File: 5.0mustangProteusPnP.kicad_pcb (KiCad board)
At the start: 2 copper layers, 139.7 x 111.1 mm, 6 parts, among them J2 5103308-3, J3 776228-1, J4 5103308-3, J5 776231-2, J6 776231-1, U1 FORD60PIN

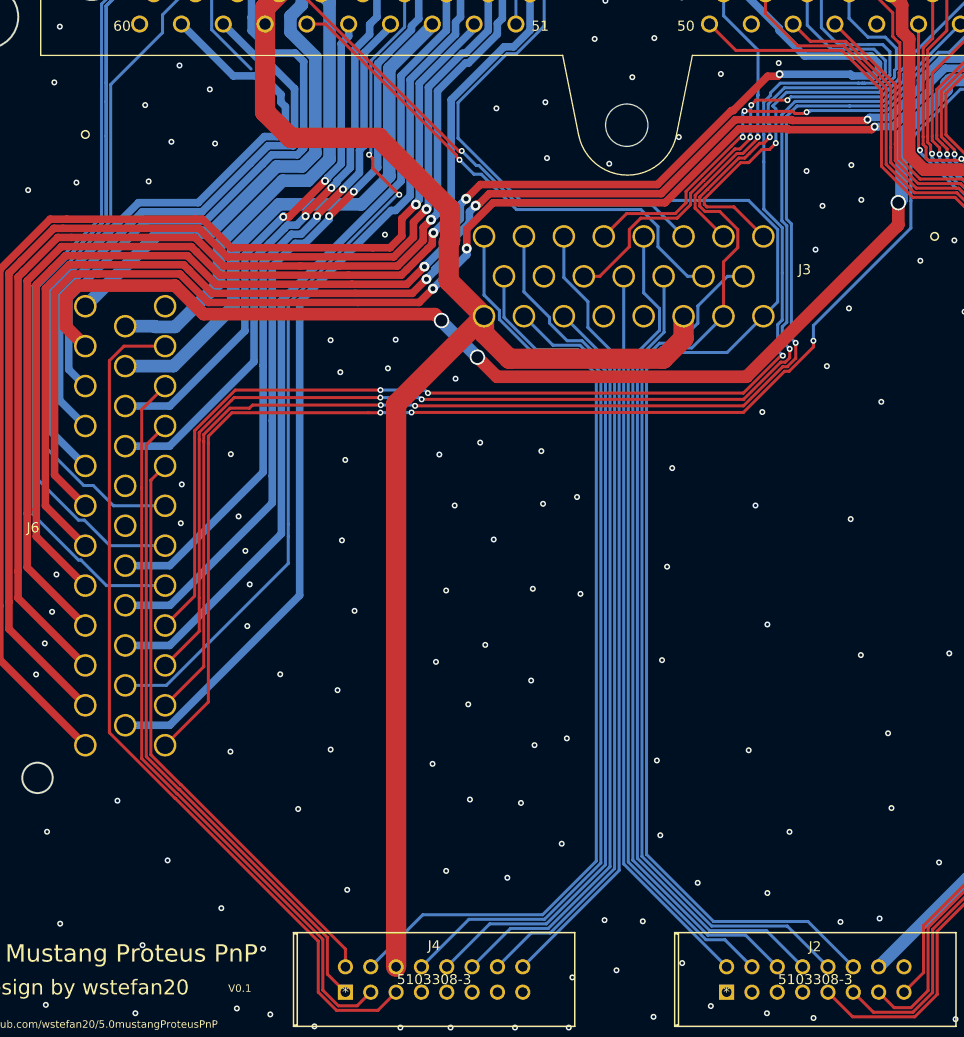
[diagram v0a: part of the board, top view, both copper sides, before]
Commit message: re-routed to optimise
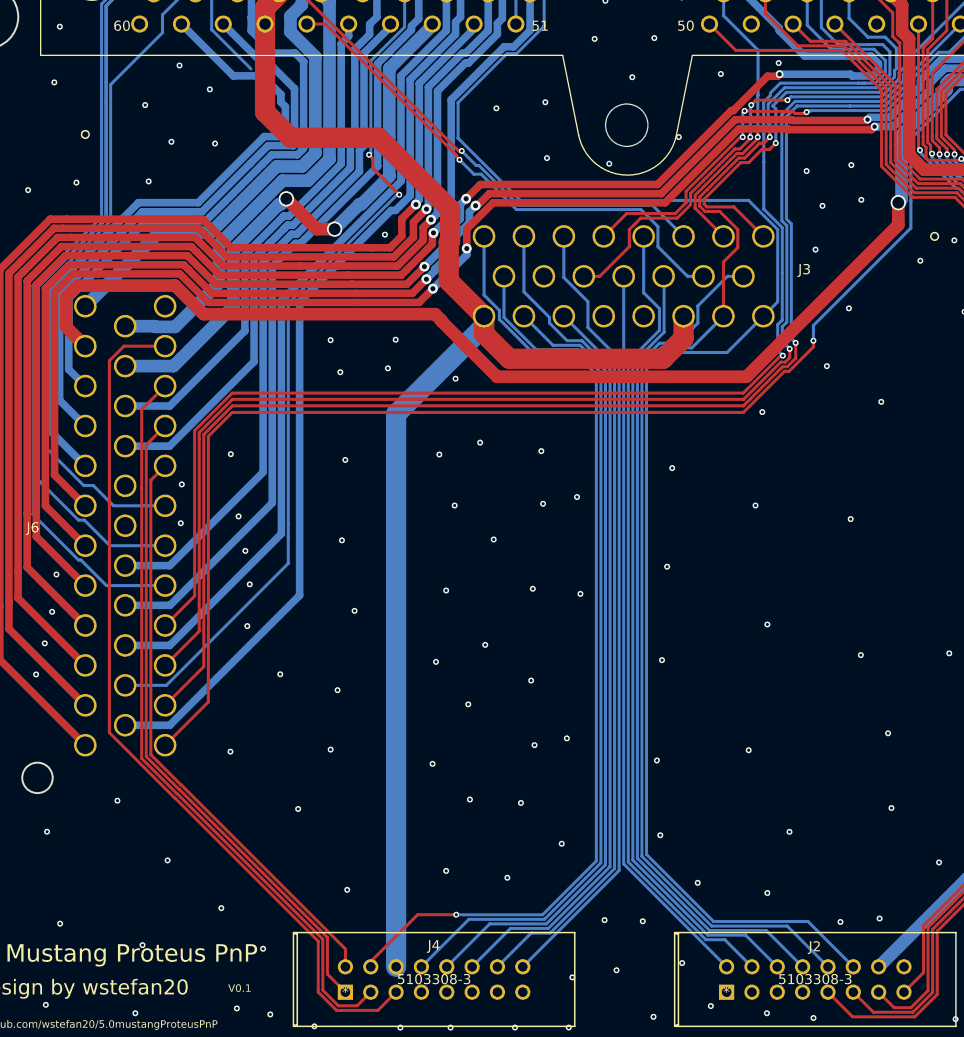
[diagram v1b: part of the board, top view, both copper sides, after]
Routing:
- net /HS4: track 54.7 -> 57.2 mm, vias 0 -> 2
- net /ETB2-: track 96.7 -> 97.0 mm, vias 0 -> 1
- net /LS10: track 79.7 -> 79.4 mm, vias 2 -> 0
- net /LS8: track 68.5 -> 68.2 mm, vias 2 -> 0
- net /IGN5: track 136.9 -> 136.7 mm, vias 3 -> 1
- net /LS4: track 62.0 -> 61.7 mm, vias 2 -> 0
- net /IGN4: track 137.6 -> 137.5 mm, vias 3 -> 1
- net /LS2: track 50.7 -> 50.6 mm, vias 2 -> 0
- net /IGN2: track 137.6 -> 137.5 mm, vias 3 -> 1
- net /IGN1: vias 3 -> 1
- net /HS1: vias 3 -> 1

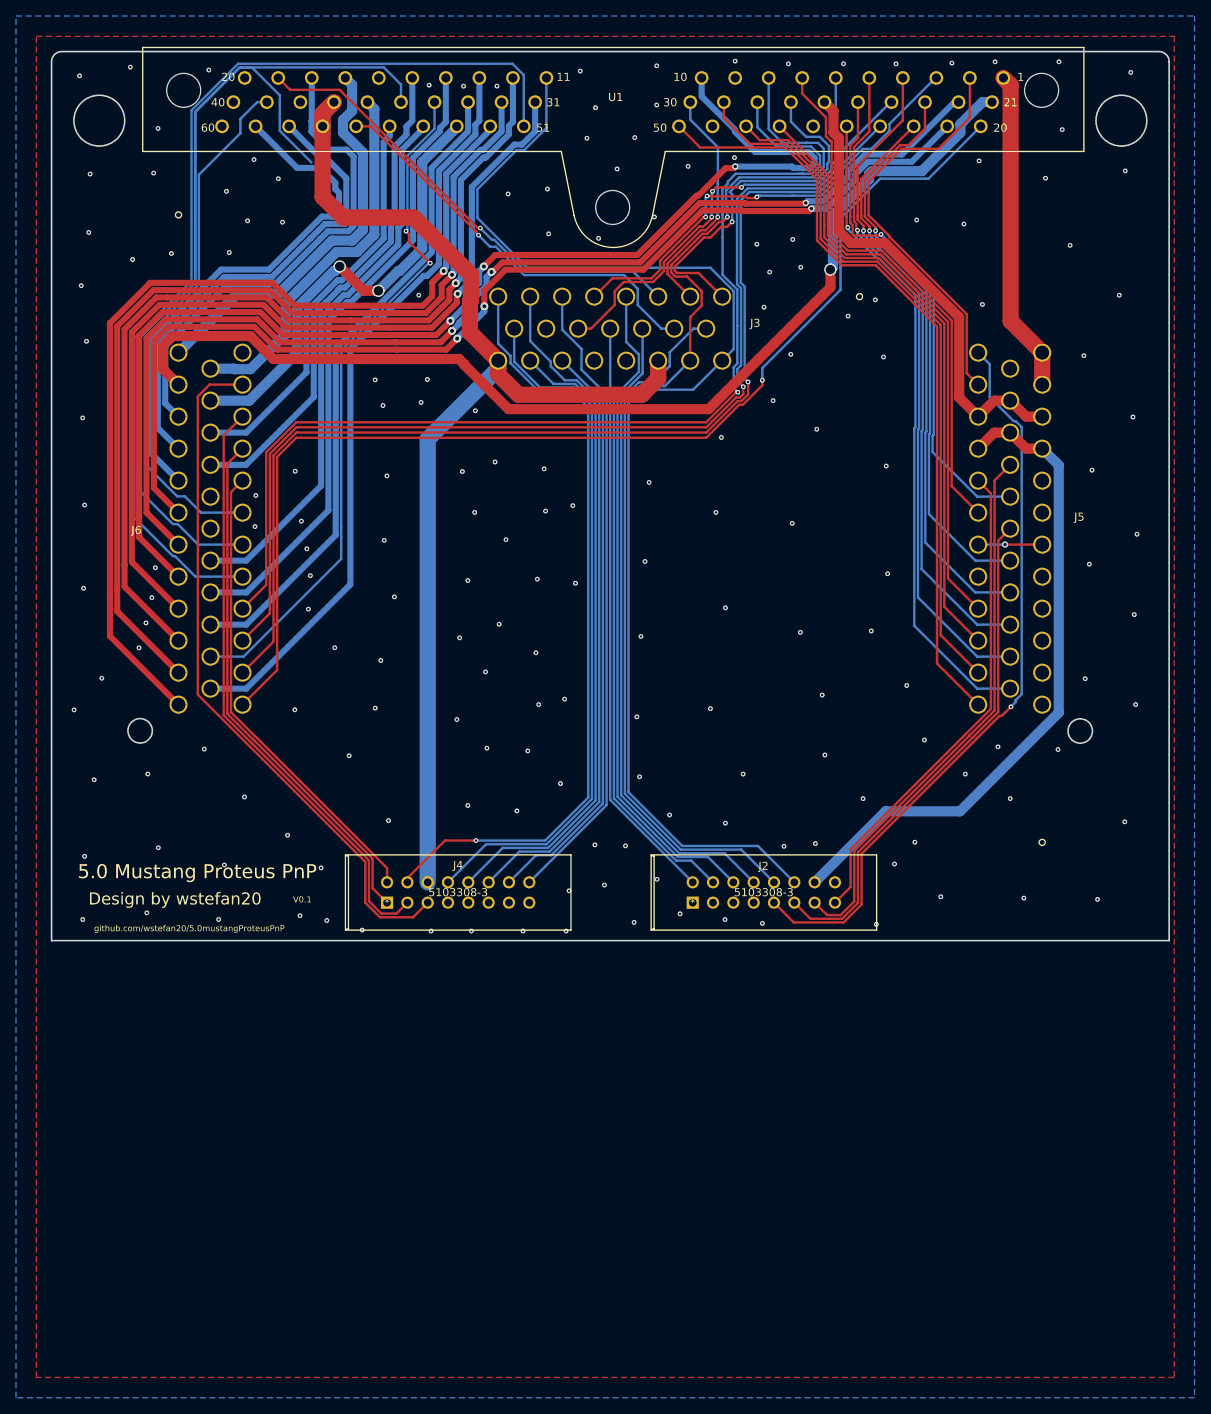
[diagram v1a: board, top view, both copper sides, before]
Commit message: changed 12V
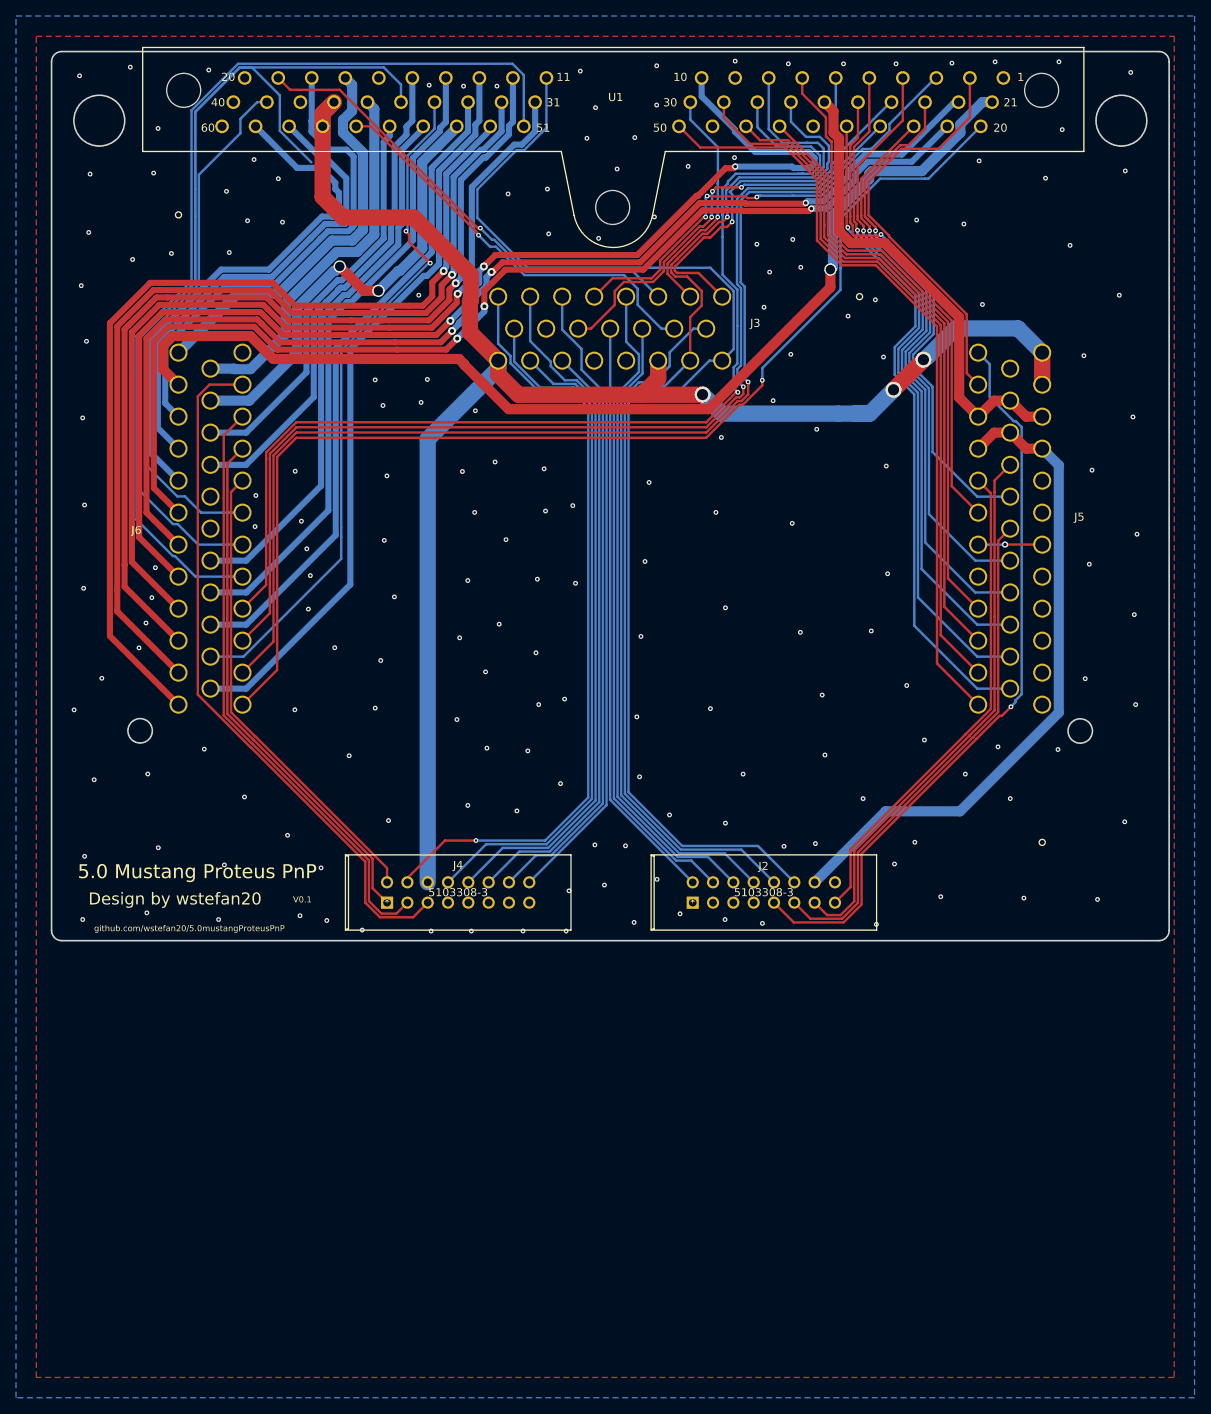
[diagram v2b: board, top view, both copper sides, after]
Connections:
- J5 pad 11: /12V -> /12V_MR
- J5 pad 12: /12V -> /12V_MR
- U1 pad 1: /12V -> (no net)
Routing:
- net /12V_MR: track 142.0 -> 204.0 mm, vias 0 -> 3
- net /12V: track 40.3 -> 0.00 mm
- net /AT1: track 62.7 -> 64.7 mm
- net /AV9: track 71.4 -> 73.4 mm
- net /AV7: track 71.5 -> 73.5 mm
- net /AV5: track 81.3 -> 83.3 mm
- net /AV3: track 83.9 -> 85.9 mm
- net /AV1: track 81.4 -> 83.5 mm
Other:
- outline, holes or cut-outs redrawn

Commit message: fixed 12V and IAC
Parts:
- added J1: 5-146280-3, 5-146280-3:5-146280-3, F.Cu at (222.3, 77.6)
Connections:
- J5 pad 11: /12V_MR -> /MR_INPUT
- J5 pad 12: /12V_MR -> /MR_INPUT
- J6 pad 2: /HS1 -> (no net)
- U1 pad 1: (no net) -> /12V
- U1 pad 21: /HS1 -> /LS14
- U1 pad 32: /LS14 -> (no net)
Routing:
- net /HS1: track 135.6 -> 0.00 mm, vias 1 -> 0
- net /LS14: track 118.6 -> 180.1 mm, vias 1 -> 2
- net /MR_INPUT: track 0.00 -> 27.0 mm
- net /12V: track 0.00 -> 14.5 mm
- net /12V_MR: track 204.0 -> 211.8 mm
- net /LS13: track 117.4 -> 118.0 mm
- net GND: vias 183 -> 204
- net (no net): vias 4 -> 0

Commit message: fixed CEL assign
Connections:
- J2 pad 1: (no net) -> /HS1
- J4 pad 7: (no net) -> /HS2
- J6 pad 2: (no net) -> /HS1
- U1 pad 17: /HS2 -> /LS12
- U1 pad 33: /LS12 -> (no net)
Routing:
- net /HS1: track 0.00 -> 125.7 mm, vias 0 -> 2
- net /HS2: track 50.3 -> 149.3 mm, vias 0 -> 1
- net /IGN7: track 147.9 -> 132.9 mm
- net /LS12: track 81.3 -> 84.1 mm, vias 0 -> 2
- net /HS4: track 57.2 -> 57.8 mm
- net GND: vias 204 -> 205

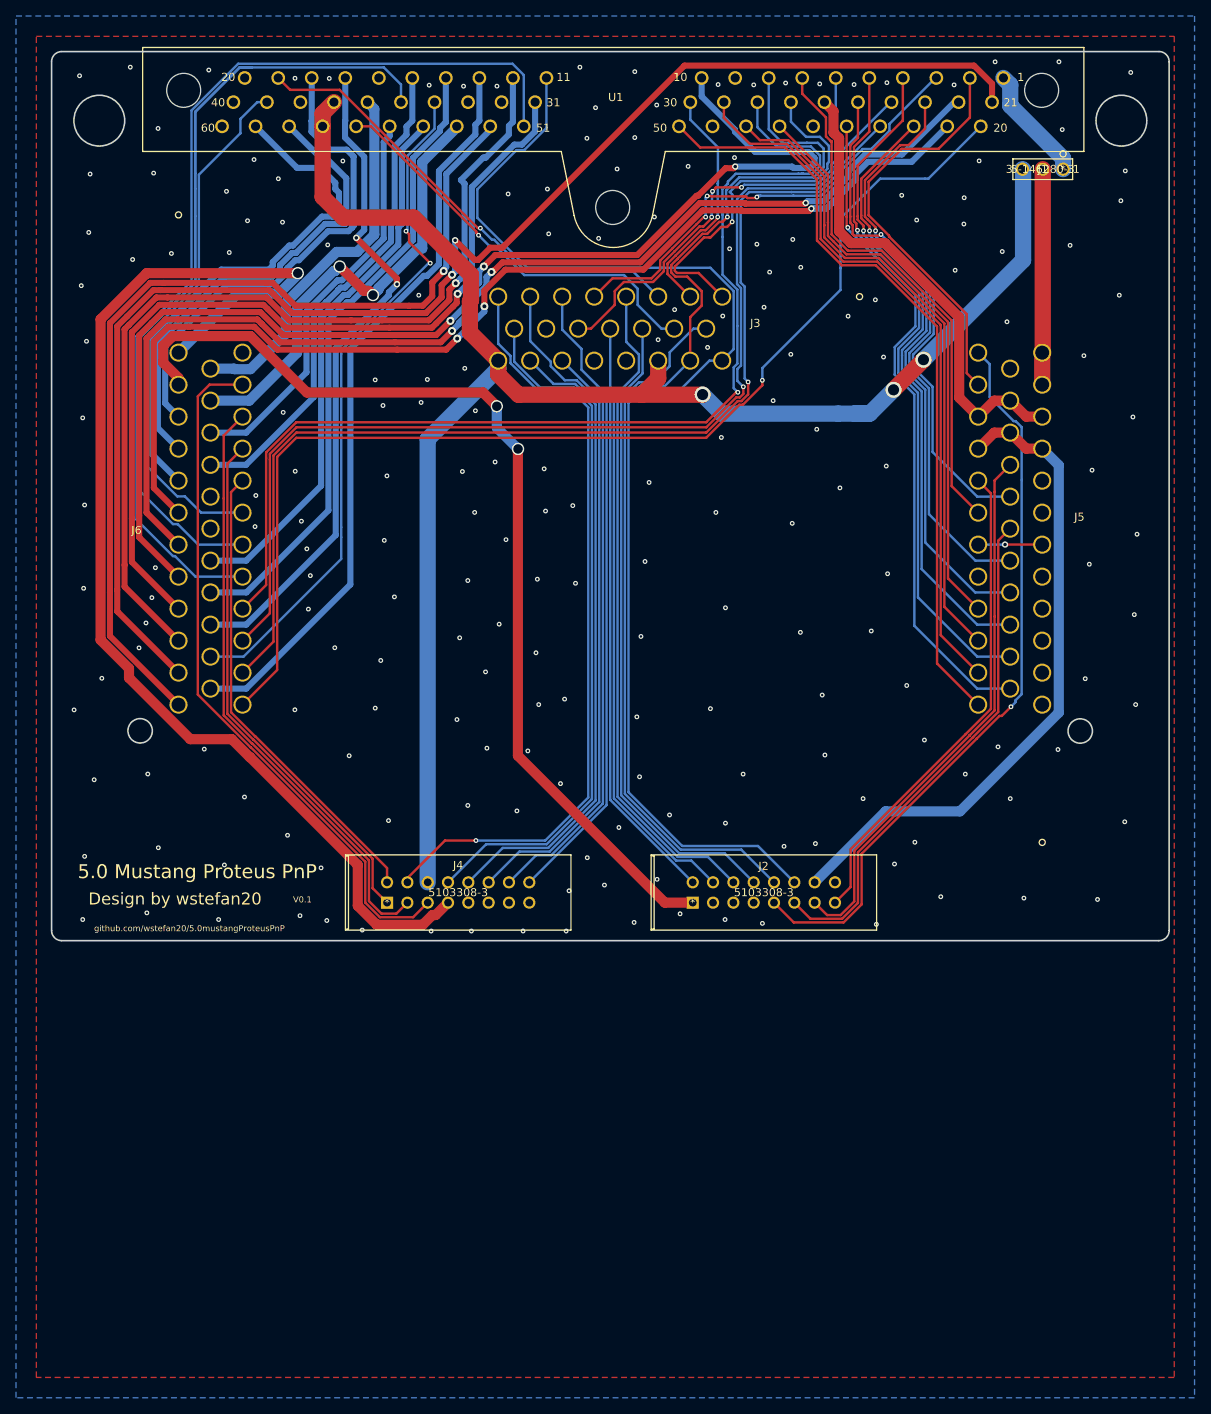
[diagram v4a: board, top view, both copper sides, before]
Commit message: updated board outline/holes
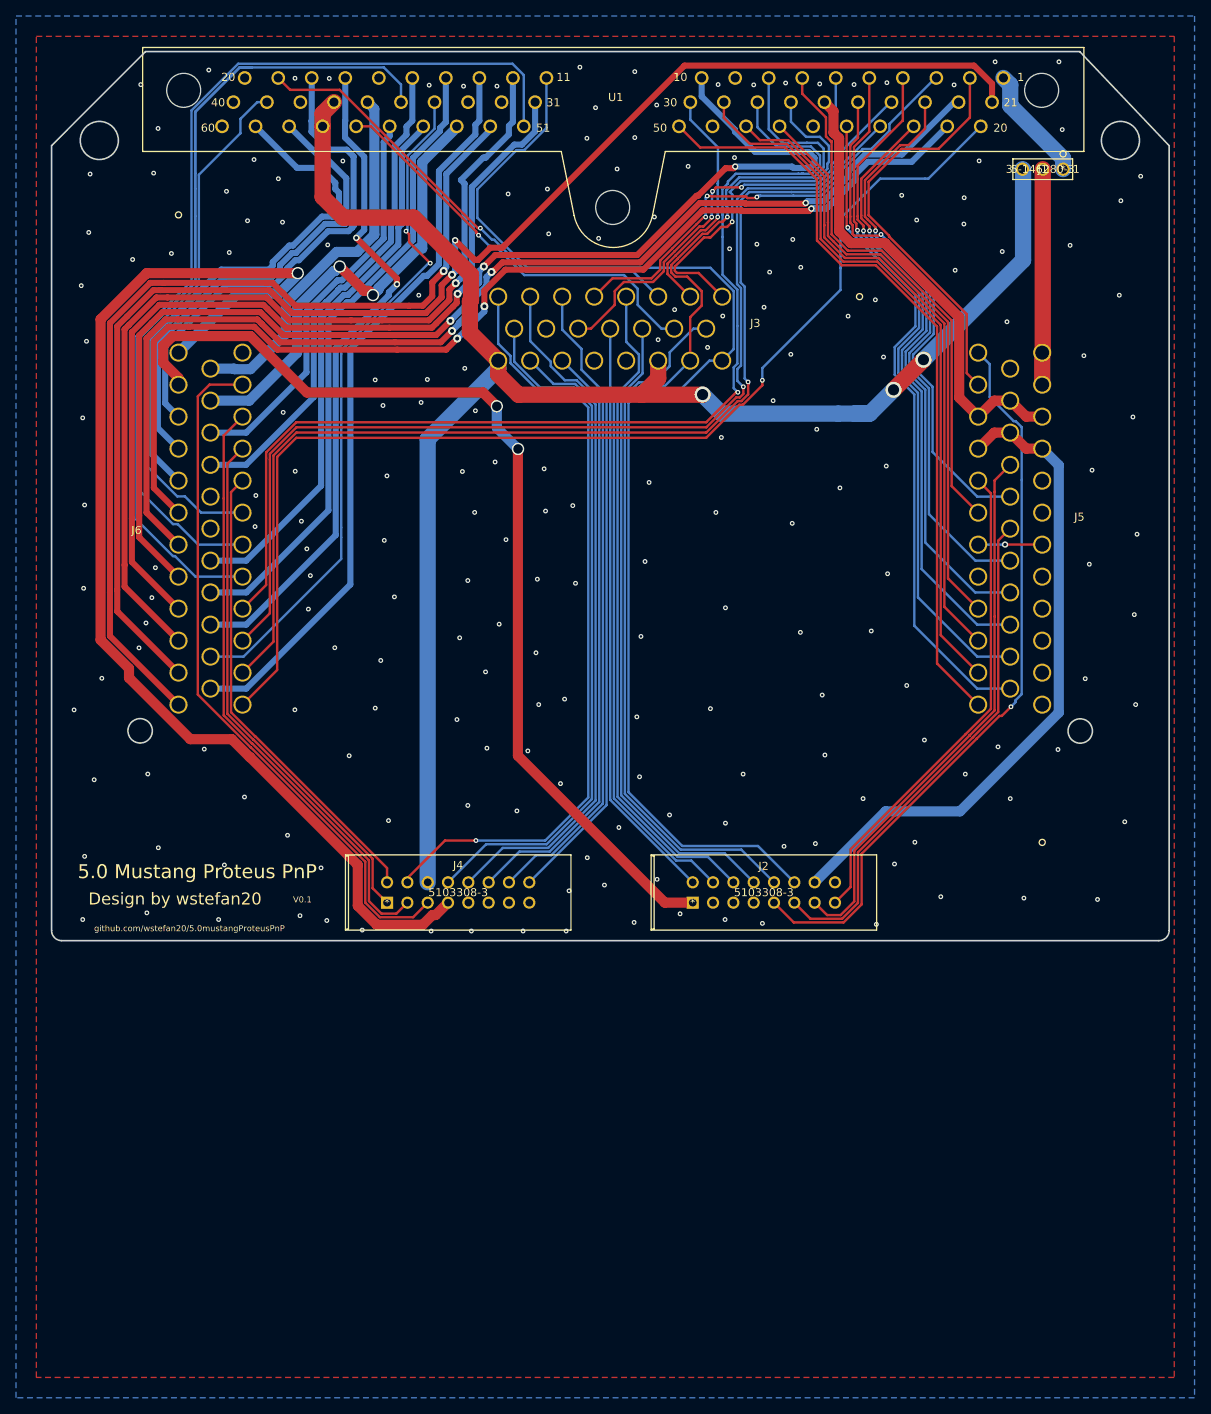
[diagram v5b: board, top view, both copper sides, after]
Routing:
- net GND: vias 205 -> 203
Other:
- outline, holes or cut-outs redrawn
